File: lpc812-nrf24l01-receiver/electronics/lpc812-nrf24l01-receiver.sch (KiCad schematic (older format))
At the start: 21 parts, among them K1 BAT, K2 CH3, K3 TH, K4 ST, P1 NRF24L01+, SW1 BIND/ISP, U1 MCP1703, U2 LPC812, X1 16MHz

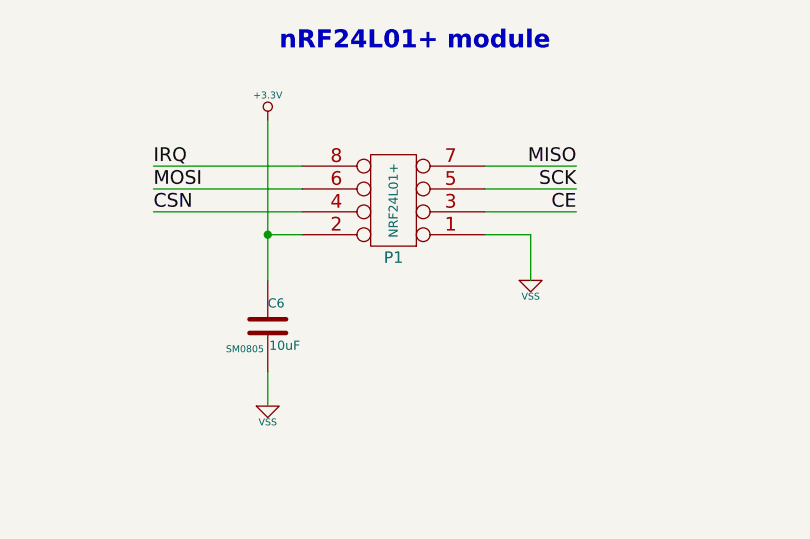
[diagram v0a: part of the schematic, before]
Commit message: Add 100uF cap against brown-out, add pull-down to prevent floating MISO
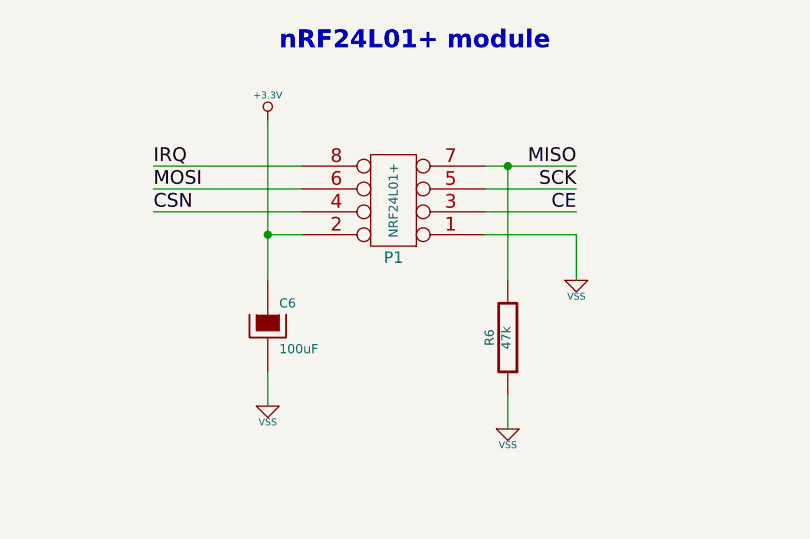
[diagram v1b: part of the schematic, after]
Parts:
- removed C6: 10uF, SM0805, symbol C
- added C6: 100uF, ~, symbol CP
- added R6: 47k, ~, symbol R
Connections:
- net +3.3V: now also C6.1
- net MISO: now also R6.2
- net VSS: now also C6.2, R6.1
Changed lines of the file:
@@
 Sheet 1 1
 Title "LPC812 / NRF24L01+ RC receiver"
-Date "27 nov 2014"
+Date "5 jan 2015"
 Rev "1"
 Comp "LANE Boys RC"
@@
 L VSS #PWR09
 U 1 1 546EE3F9
-P 8550 5950
-F 0 "#PWR09" H 8550 5950 30  0001 C CNN
-F 1 "VSS" H 8550 5880 30  0000 C CNN
-F 2 "" H 8550 5950 60  0000 C CNN
-F 3 "" H 8550 5950 60  0000 C CNN
-	1    8550 5950
+P 8750 5950
+F 0 "#PWR09" H 8750 5950 30  0001 C CNN
+F 1 "VSS" H 8750 5880 30  0000 C CNN
+F 2 "" H 8750 5950 60  0000 C CNN
+F 3 "" H 8750 5950 60  0000 C CNN
+	1    8750 5950
 	1    0    0    -1
 $EndComp
@@
 	5950 2150 6650 2150
 Wire Wire Line
-	8350 5750 8550 5750
-Wire Wire Line
-	8550 5750 8550 5950
+	8350 5750 8750 5750
 Wire Wire Line
 	7400 5250 7400 5950
@@
 	9450 1500 9750 1500
 Connection ~ 9750 1500
-$Comp
-L C C6
-U 1 1 5471B4BB
-P 7400 6150
-F 0 "C6" H 7400 6250 40  0000 L CNN
-F 1 "10uF" H 7406 6065 40  0000 L CNN
-F 2 "SM0805" H 7300 6050 30  0000 C CNN
-F 3 "~" H 7400 6150 60  0000 C CNN
-	1    7400 6150
-	1    0    0    -1
-$EndComp
 Connection ~ 7400 5750
 $Comp
@@
 Wire Wire Line
 	4300 4500 4900 4500
+$Comp
+L CP C6
+U 1 1 54A9F170
+P 7400 6150
+F 0 "C6" H 7450 6250 40  0000 L CNN
+F 1 "100uF" H 7450 6050 40  0000 L CNN
+F 2 "~" H 7500 6000 30  0000 C CNN
+F 3 "~" H 7400 6150 300 0000 C CNN
+	1    7400 6150
+	1    0    0    -1
+$EndComp
+$Comp
+L R R6
+U 1 1 54A9F5EB
+P 8450 6200
+F 0 "R6" V 8530 6200 40  0000 C CNN
+F 1 "47k" V 8457 6201 40  0000 C CNN
+F 2 "~" V 8380 6200 30  0000 C CNN
+F 3 "~" H 8450 6200 30  0000 C CNN
+	1    8450 6200
+	-1   0    0    1
+$EndComp
+Wire Wire Line
+	8750 5750 8750 5950
+$Comp
+L VSS #PWR021
+U 1 1 54A9F674
+P 8450 6600
+F 0 "#PWR021" H 8450 6600 30  0001 C CNN
+F 1 "VSS" H 8450 6530 30  0000 C CNN
+F 2 "" H 8450 6600 60  0000 C CNN
+F 3 "" H 8450 6600 60  0000 C CNN
+	1    8450 6600
+	1    0    0    -1
+$EndComp
+Wire Wire Line
+	8450 6450 8450 6600
+Wire Wire Line
+	8450 5950 8450 5450
+Connection ~ 8450 5450
 $EndSCHEMATC
